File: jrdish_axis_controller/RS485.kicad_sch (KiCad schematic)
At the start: 50 parts, among them CN3 KF2EDGR-2.54-4P, CN4 KF2EDGR-2.54-4P, CN5 KF2EDGR-2.54-4P, U2 ISOW1432BDFMR, U3 ISOW1432BDFMR

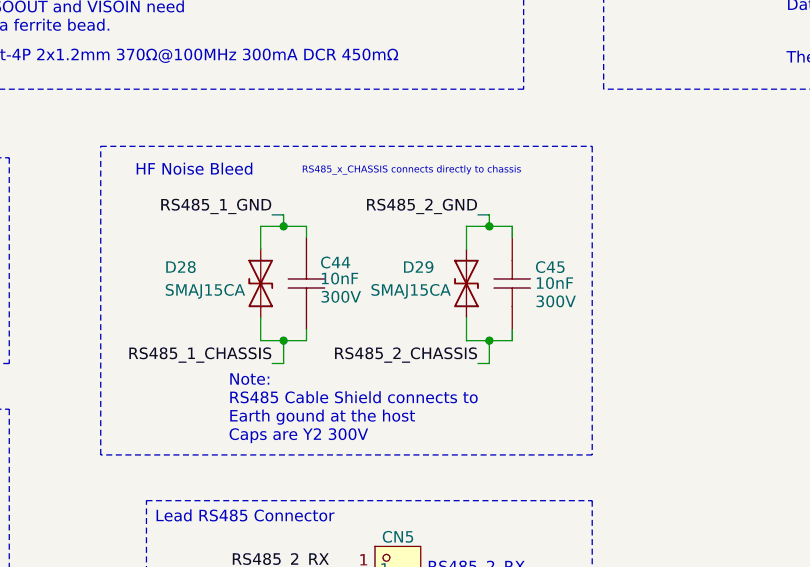
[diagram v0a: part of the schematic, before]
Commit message: Updates for replacing 10k resistors and encoder RC.
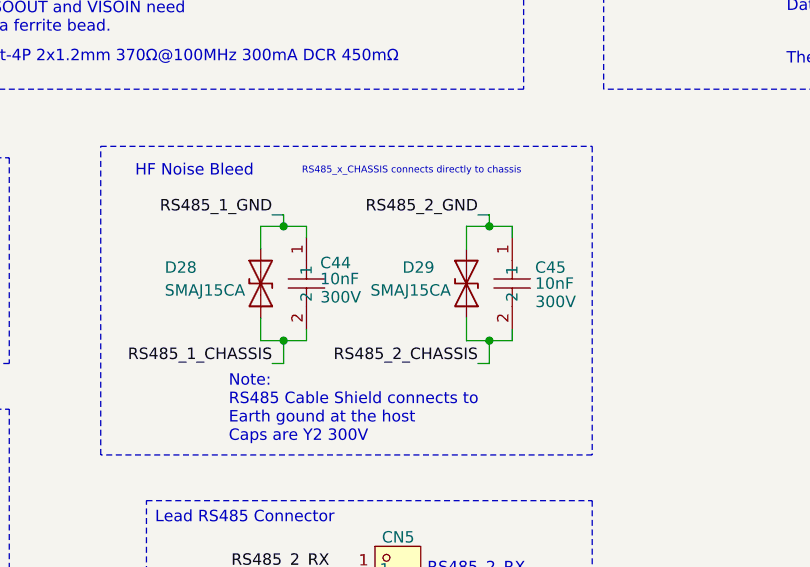
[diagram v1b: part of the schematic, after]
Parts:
- D27, D30: KiLib_Generator (none) -> package/gullwing
- R18, R19: Field4 (none) -> ${REFERENCE}
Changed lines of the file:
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@@
 	(title_block
 		(title "RS485")
-		(date "2026-04-30")
-		(rev "1.0")
+		(date "2026-07-11")
+		(rev "1.1")
 		(company "JRSeti")
 	)
@@
 	)
 	(symbol
-		(lib_name "C43Q1103K40C80F_2")
 		(lib_id "MyParts:C43Q1103K40C80F")
 		(at 118.11 135.89 90)
@@
 			)
 		)
+		(property "KiLib_Generator" "package/gullwing"
+			(at 245.11 31.75 0)
+			(hide yes)
+			(show_name no)
+			(do_not_autoplace no)
+			(effects
+				(font
+					(size 1.27 1.27)
+				)
+			)
+		)
 		(pin "2"
 		)
@@
 			)
 		)
+		(property "KiLib_Generator" "package/gullwing"
+			(at 76.2 31.75 0)
+			(hide yes)
+			(show_name no)
+			(do_not_autoplace no)
+			(effects
+				(font
+					(size 1.27 1.27)
+				)
+			)
+		)
 		(pin "2"
 		)
@@
 	)
 	(symbol
-		(lib_name "C43Q1103K40C80F_1")
 		(lib_id "MyParts:C43Q1103K40C80F")
 		(at 140.97 135.89 90)
@@
 			)
 		)
+		(property "Field4" "${REFERENCE}"
+			(at 24.13 52.07 0)
+			(hide yes)
+			(show_name no)
+			(do_not_autoplace no)
+			(effects
+				(font
+					(size 1.27 1.27)
+				)
+			)
+		)
 		(pin "1"
 		)
@@
 			)
 		)
-		(property "Datasheet" "https://www.ti.com/lit/ds/symlink/isow1432.pdf?ts=1648465263803&ref_url=https%253A%252F%252Fwww.google.com%252F"
+		(property "Datasheet" "https://www.lcsc.com/datasheet/C5216543.pdf"
 			(at 86.36 78.74 0)
 			(hide yes)
@@
 			)
 		)
+		(property "Field4" "${REFERENCE}"
+			(at 160.02 52.07 0)
+			(hide yes)
+			(show_name no)
+			(do_not_autoplace no)
+			(effects
+				(font
+					(size 1.27 1.27)
+				)
+			)
+		)
 		(pin "1"
 		)
@@
 			)
 		)
-		(property "Datasheet" "https://www.ti.com/lit/ds/symlink/isow1432.pdf?ts=1648465263803&ref_url=https%253A%252F%252Fwww.google.com%252F"
+		(property "Datasheet" "https://www.lcsc.com/datasheet/C5216543.pdf"
 			(at 222.25 78.74 0)
 			(hide yes)
